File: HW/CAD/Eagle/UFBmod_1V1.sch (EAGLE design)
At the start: 87 parts, among them U101 DIGILENT_CMOD_A7, U301 MAX5217, U401 AT86RF215-ZU, U411 ASVTX-13-D-26.000MHZ-I05-T, U511 PE4259, U521 RFX1010, U581 B39871B3440U410, U611 TPS62056DGSR, X221 TTE_EN11-HSM, X591 ANTENNATINY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

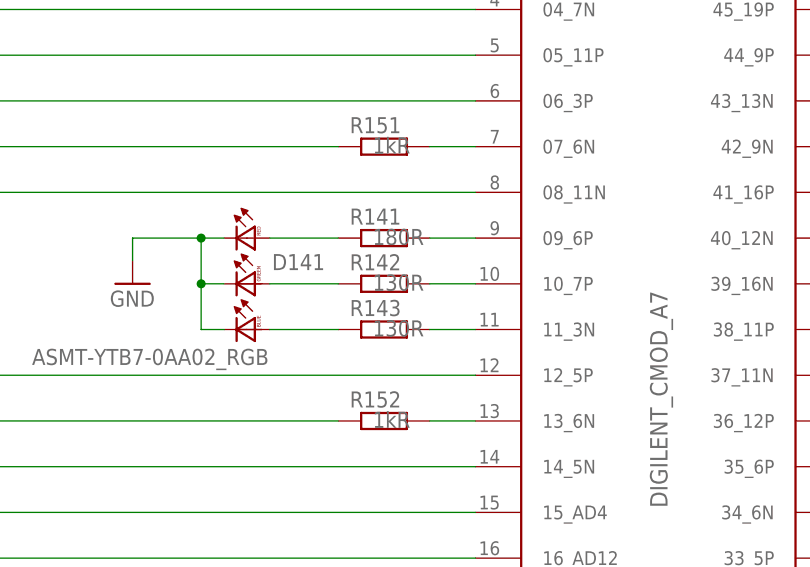
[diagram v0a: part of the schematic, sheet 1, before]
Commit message: HW_1V1 - CAD/Eagle - LED resistors changed
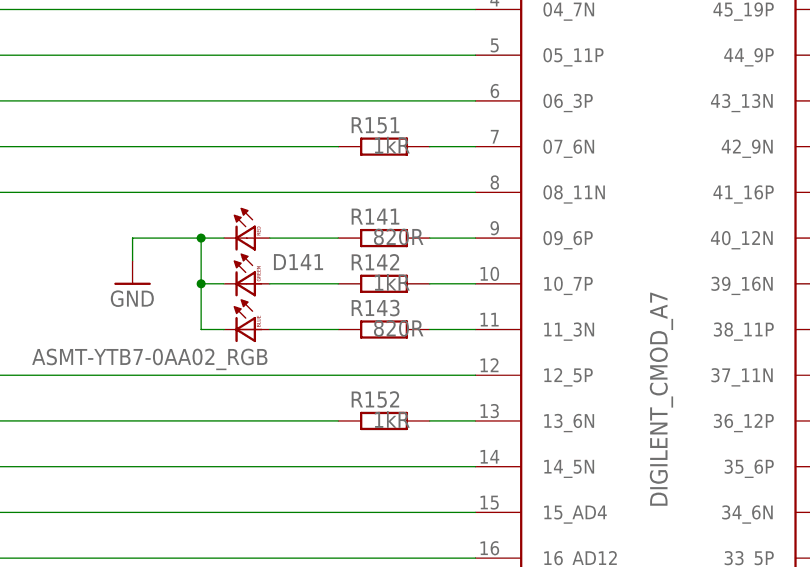
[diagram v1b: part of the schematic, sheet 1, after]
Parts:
- R141: value 180R -> 820R
- R142: value 130R -> 1kR
- R143: value 130R -> 820R
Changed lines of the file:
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@@
 <part name="R734" library="df4iah_rcl" deviceset="R-EU_" device="R0402" value="100R"/>
 <part name="R733" library="df4iah_rcl" deviceset="R-EU_" device="R0402" value="100R"/>
-<part name="R141" library="df4iah_rcl" deviceset="R-EU_" device="R0402" value="180R"/>
-<part name="R142" library="df4iah_rcl" deviceset="R-EU_" device="R0402" value="130R"/>
-<part name="R143" library="df4iah_rcl" deviceset="R-EU_" device="R0402" value="130R"/>
+<part name="R141" library="df4iah_rcl" deviceset="R-EU_" device="R0402" value="820R"/>
+<part name="R142" library="df4iah_rcl" deviceset="R-EU_" device="R0402" value="1kR"/>
+<part name="R143" library="df4iah_rcl" deviceset="R-EU_" device="R0402" value="820R"/>
 <part name="D141" library="df4iah_led" deviceset="ASMT-YTB7-0AA02_RGB" device=""/>
 <part name="GND141" library="df4iah_supply" deviceset="GND" device=""/>

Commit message: HW_1V1 - CAD/Eagle - LED wire names exchanged
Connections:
- net LED_B: now also R143.2, U101.11_3N; no longer D141.BA, R143.1
- net LED_B_R: now also D141.BA, R143.1; no longer R143.2, U101.11_3N
- net LED_G: now also R142.2, U101.10_7P; no longer D141.GA, R142.1
- net LED_G_R: now also D141.GA, R142.1; no longer R142.2, U101.10_7P
- net LED_R: now also R141.2, U101.09_6P; no longer D141.RA, R141.1
- net LED_R_R: now also D141.RA, R141.1; no longer R141.2, U101.09_6P
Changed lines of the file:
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@@
 </segment>
 </net>
-<net name="LED_G_R" class="0">
+<net name="LED_G" class="0">
 <segment>
 <pinref part="U101" gate="G$1" pin="10_7P"/>
@@
 </segment>
 </net>
-<net name="LED_B_R" class="0">
+<net name="LED_B" class="0">
 <segment>
 <pinref part="U101" gate="G$1" pin="11_3N"/>
@@
 </segment>
 </net>
-<net name="LED_R" class="0">
+<net name="LED_R_R" class="0">
 <segment>
 <pinref part="R141" gate="G$1" pin="1"/>
@@
 </segment>
 </net>
-<net name="LED_G" class="0">
+<net name="LED_G_R" class="0">
 <segment>
 <pinref part="R142" gate="G$1" pin="1"/>
@@
 </segment>
 </net>
-<net name="LED_B" class="0">
+<net name="LED_B_R" class="0">
 <segment>
 <pinref part="R143" gate="G$1" pin="1"/>
@@
 </segment>
 </net>
-<net name="LED_R_R" class="0">
+<net name="LED_R" class="0">
 <segment>
 <pinref part="U101" gate="G$1" pin="09_6P"/>
